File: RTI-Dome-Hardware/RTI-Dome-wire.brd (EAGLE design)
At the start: 80 x 71.1 mm, 33 parts, among them IC2 74LVC244

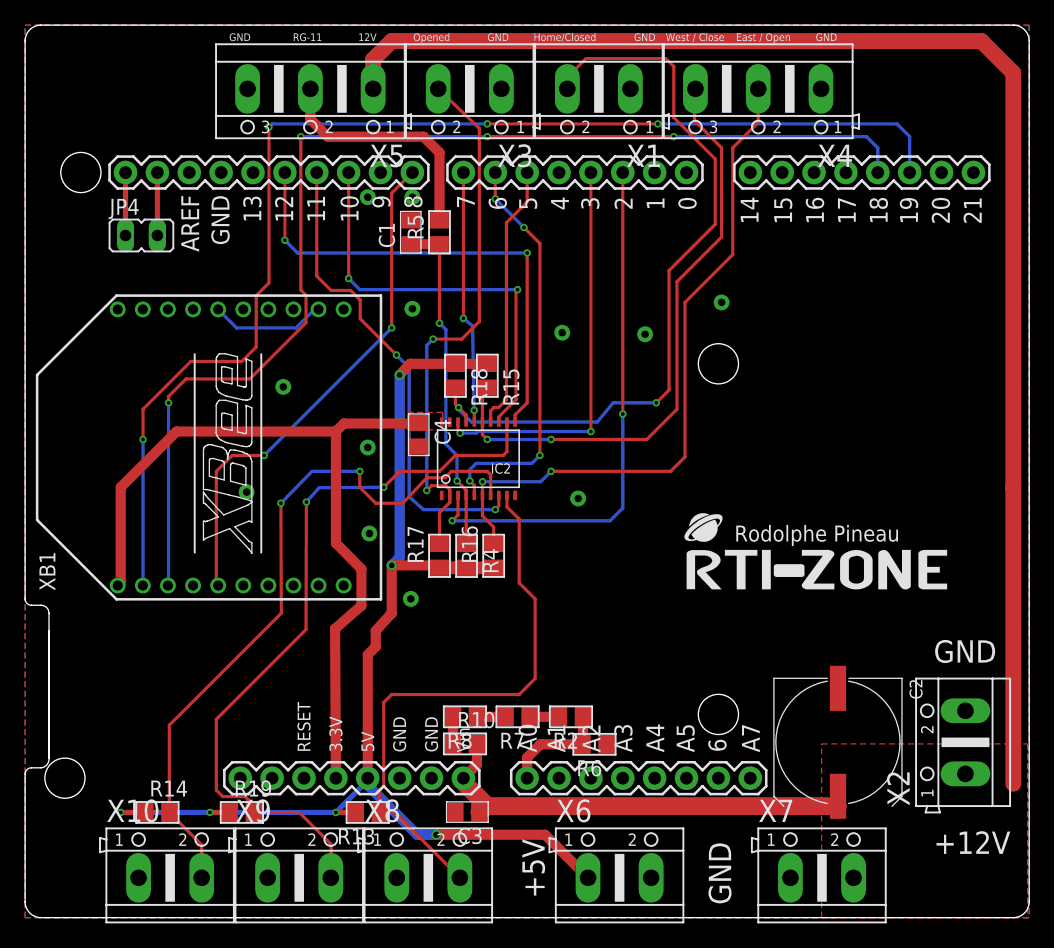
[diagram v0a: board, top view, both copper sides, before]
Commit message: Fix some components positions
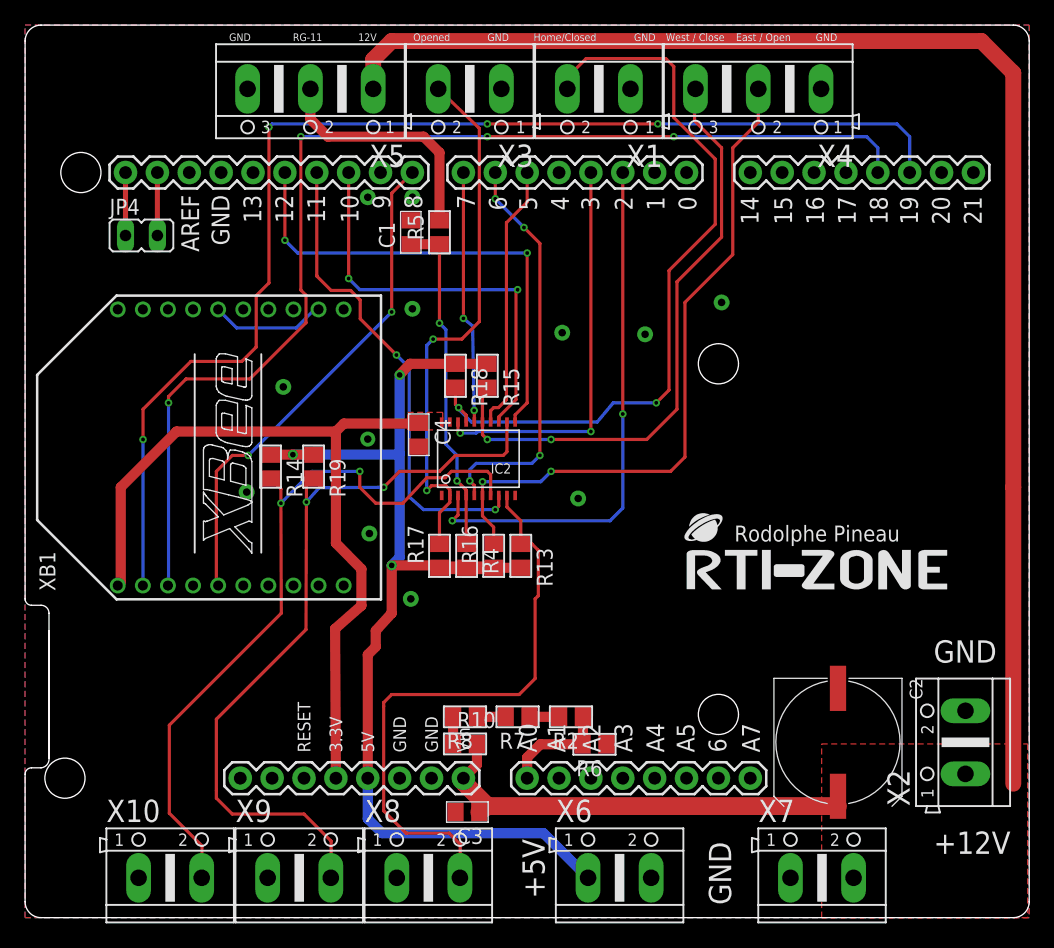
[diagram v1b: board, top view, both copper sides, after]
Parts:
- moved R14 29.0 mm to (19.6, 35.9), turned to 270 degrees
- moved R19 28.1 mm to (23.0, 35.9), turned to 270 degrees
- moved R13 23.8 mm to (39.5, 28.8), turned to 270 degrees
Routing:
- net VCC: track 95.8 -> 85.6 mm, vias 6 -> 3
- net M_DIR_5V: track 59.9 -> 62.2 mm
- net M_STEP_5V: track 45.8 -> 47.6 mm
- net M_EN_5V: track 60.3 -> 59.4 mm
- net XBEE_RESET: track 40.9 -> 40.2 mm

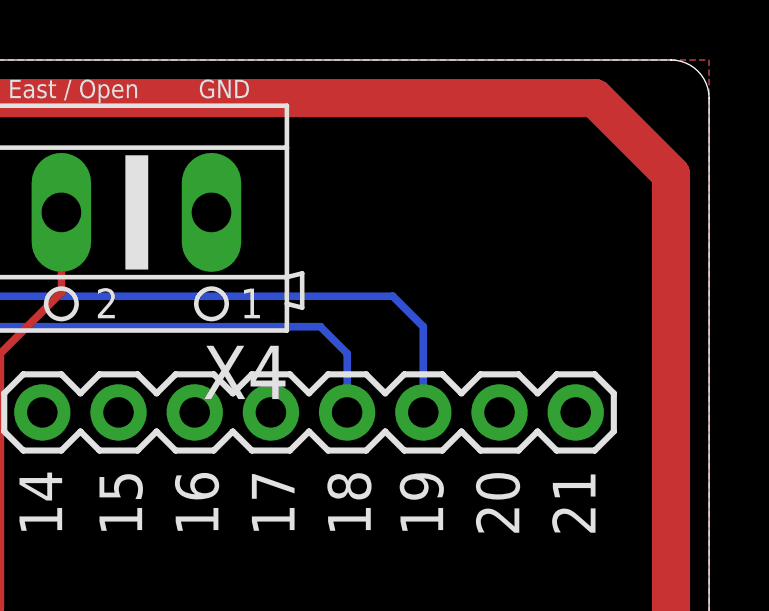
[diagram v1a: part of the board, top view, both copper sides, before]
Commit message: Stop interrupt in motor disable code.
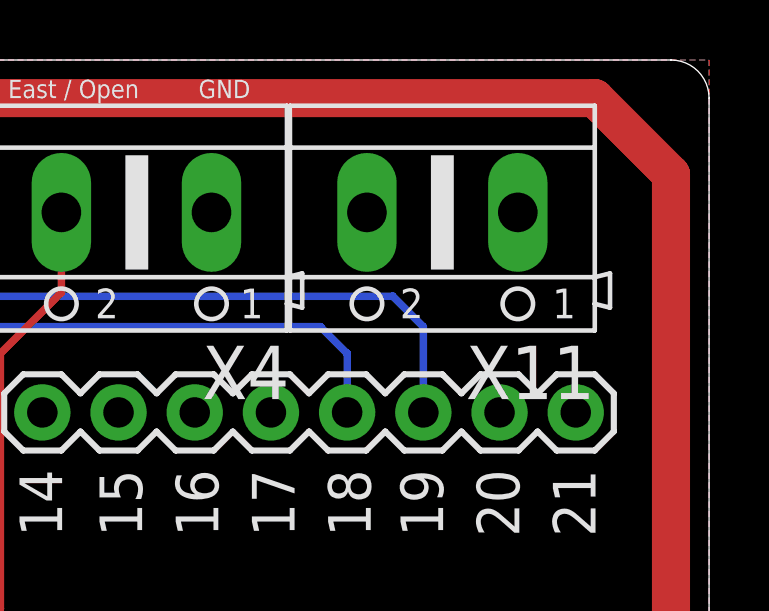
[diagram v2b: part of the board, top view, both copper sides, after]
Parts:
- added X11: (no value), con-ptr500:AK500/2
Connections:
- new net AT_PARK_PIN: PCB1.A5, X11.1
- new net AT_PARK_PIN_LOOP: PCB1.A4, X11.2
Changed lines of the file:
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@@
 <attribute name="OC_FARNELL" value="unknown" x="11.557" y="3.175" size="1.778" layer="27" display="off"/>
+</element>
+<element name="X11" library="con-ptr500" package="AK500/2" value="" x="71.12" y="66.04" rot="R180">
+<attribute name="MF" value="" x="71.12" y="66.04" size="1.778" layer="27" rot="R180" display="off"/>
+<attribute name="OC_NEWARK" value="unknown" x="71.12" y="66.04" size="1.778" layer="27" rot="R180" display="off"/>
+<attribute name="MPN" value="" x="71.12" y="66.04" size="1.778" layer="27" rot="R180" display="off"/>
+<attribute name="OC_FARNELL" value="unknown" x="71.12" y="66.04" size="1.778" layer="27" rot="R180" display="off"/>
 </element>
 </elements>
@@
 <wire x1="40.193" y1="16.002" x2="42.5475" y2="16.002" width="0.8128" layer="1"/>
 </signal>
+<signal name="AT_PARK_PIN_LOOP">
+<contactref element="X11" pad="2"/>
+<contactref element="PCB1" pad="A4"/>
+<wire x1="68.6054" y1="66.04" x2="50.165" y2="11.1125" width="0" layer="19" extent="1-1"/>
+</signal>
+<signal name="AT_PARK_PIN">
+<contactref element="X11" pad="1"/>
+<contactref element="PCB1" pad="A5"/>
+<wire x1="73.6346" y1="66.04" x2="52.705" y2="11.1125" width="0" layer="19" extent="1-1"/>
+</signal>
 </signals>

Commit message: Started adding some extra connection.. for dual shutter systems.
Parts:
- moved R6 6.13 mm to (39.2, 13.8), turned to 0 degrees
- moved R2 1.46 mm to (42.4, 15.0), turned to 90 degrees
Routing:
- net VPIN: track 8.70 -> 5.13 mm
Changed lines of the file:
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@@
 <setting verticaltext="up"/>
 </settings>
-<grid distance="0.127" unitdist="mm" unit="mm" style="lines" multiple="1" display="yes" altdistance="0.03175" altunitdist="mm" altunit="mm"/>
+<grid distance="1.27" unitdist="mm" unit="mm" style="lines" multiple="1" display="yes" altdistance="0.03175" altunitdist="mm" altunit="mm"/>
 <layers>
 <layer number="1" name="Top" color="4" fill="1" visible="yes" active="yes"/>
@@
 <element name="R18" library="rti" package="R0805" value="4.7K" x="34.29" y="43.18" rot="R270"/>
 <element name="R19" library="rti" package="R0805" value="1K" x="22.987" y="35.941" rot="R270"/>
-<element name="R6" library="rti" package="R0805" value="100K 0.1%" x="45.37075" y="13.81125" rot="R180"/>
+<element name="R6" library="rti" package="R0805" value="100K 0.1%" x="39.243" y="13.843"/>
 <element name="R7" library="rti" package="R0805" value="100K 0.1%" x="39.243" y="16.002" rot="R180"/>
 <element name="R8" library="rti" package="R0805" value="100K 0.1%" x="35.052" y="16.002" rot="R180"/>
@@
 </element>
 <element name="PCB1" library="arduino_shield" package="ARDUINO_DUE_SHIELD_SHORT" value="ARDUINO_DUE_SHIELD_SHORT" x="40.005" y="32.7025"/>
-<element name="R2" library="rti" package="R0805" value="100K 0.1%" x="43.4975" y="16.002" rot="R180"/>
+<element name="R2" library="rti" package="R0805" value="100K 0.1%" x="42.418" y="15.01775" rot="R90"/>
 <element name="C3" library="rti" package="C0805" value="10uF" x="35.2425" y="8.41375" rot="R180"/>
 <element name="X7" library="con-ptr500" package="AK500/2" value="" x="63.5" y="3.175">
@@
 <contactref element="PCB1" pad="A0"/>
 <contactref element="R2" pad="1"/>
-<wire x1="44.4475" y1="16.002" x2="44.4475" y2="13.838" width="0.8128" layer="1"/>
-<wire x1="44.4475" y1="13.838" x2="44.42075" y2="13.81125" width="0.8128" layer="1"/>
-<wire x1="44.42075" y1="13.81125" x2="41.05275" y2="13.81125" width="0.8128" layer="1"/>
-<wire x1="41.05275" y1="13.81125" x2="40.005" y2="12.7635" width="0.8128" layer="1"/>
-<wire x1="40.005" y1="12.7635" x2="40.005" y2="11.1125" width="0.8128" layer="1"/>
+<wire x1="40.193" y1="13.843" x2="40.193" y2="11.3005" width="0.8128" layer="1"/>
+<wire x1="40.193" y1="11.3005" x2="40.005" y2="11.1125" width="0.8128" layer="1"/>
+<wire x1="42.418" y1="14.06775" x2="40.41775" y2="14.06775" width="0.8128" layer="1"/>
+<wire x1="40.41775" y1="14.06775" x2="40.193" y2="13.843" width="0.8128" layer="1"/>
 </signal>
 <signal name="M_EN">
@@
 <contactref element="X9" pad="1"/>
 <contactref element="X10" pad="1"/>
+<via x="37.465" y="11.46175" extent="1-16" drill="0.6" diameter="1.27"/>
 </signal>
 <signal name="+12V" class="1">
@@
 <contactref element="R7" pad="1"/>
 <contactref element="R2" pad="2"/>
-<wire x1="40.193" y1="16.002" x2="42.5475" y2="16.002" width="0.8128" layer="1"/>
+<wire x1="40.193" y1="16.002" x2="42.38375" y2="16.002" width="0.8128" layer="1"/>
+<wire x1="42.38375" y1="16.002" x2="42.418" y2="15.96775" width="0.8128" layer="1"/>
 </signal>
 <signal name="AT_PARK_PIN_LOOP">
 <contactref element="X11" pad="2"/>
 <contactref element="PCB1" pad="A4"/>
-<wire x1="68.6054" y1="66.04" x2="50.165" y2="11.1125" width="0" layer="19" extent="1-1"/>
+<wire x1="50.165" y1="11.1125" x2="68.6054" y2="66.04" width="0" layer="19" extent="1-1"/>
 </signal>
 <signal name="AT_PARK_PIN">
 <contactref element="X11" pad="1"/>
 <contactref element="PCB1" pad="A5"/>
-<wire x1="73.6346" y1="66.04" x2="52.705" y2="11.1125" width="0" layer="19" extent="1-1"/>
+<wire x1="52.705" y1="11.1125" x2="73.6346" y2="66.04" width="0" layer="19" extent="1-1"/>
 </signal>
 </signals>
